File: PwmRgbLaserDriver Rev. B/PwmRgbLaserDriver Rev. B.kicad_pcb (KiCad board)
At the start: 2 copper layers, 63 x 42 mm, 55 parts, among them IC1 ADA4817-1ARDZ, IC2 ADA4817-1ARDZ, IC3 ADA4817-1ARDZ, J1 RED_IN, J2 15V, J3 RLO, J4 GREEN_IN, J5 GLO, J6 BLUE_IN, J7 BLO, Q1 Q_NPN_BCE, Q2 Q_NPN_BCE, Q3 Q_NPN_BCE, U1 TPS54331GDR

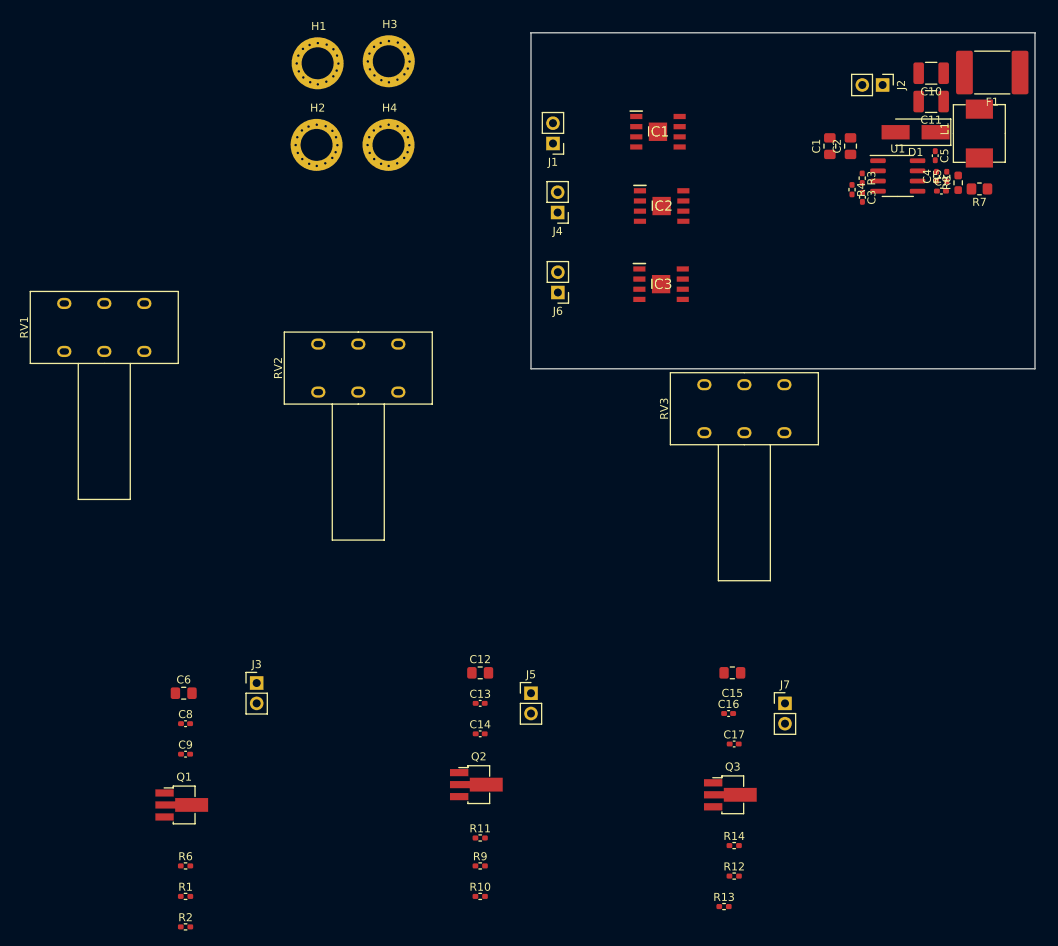
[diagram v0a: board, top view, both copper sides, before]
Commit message: Placement And Some Routhing
Placed all components and routed the important analog signal traces.
Power remains unfinished along with precise placement of the mounting holes.
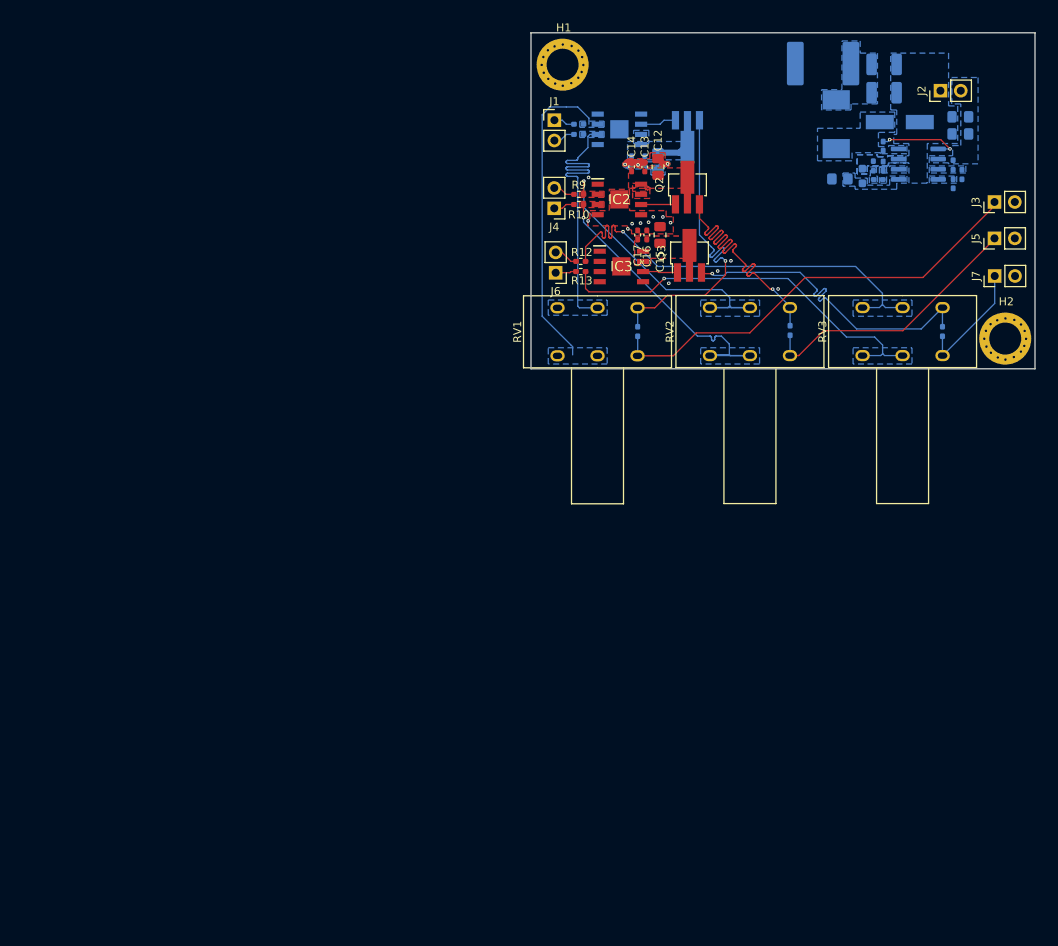
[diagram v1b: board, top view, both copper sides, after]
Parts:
- removed H3, H4: GND, SamacSys_Parts:4mm Mounting Hole
- C1, C10, C11, C2, C3, C4, C5, C6, C7, C8, C9, D1, F1, IC1, L1, Q1, R1, R11, R14, R2, R3, R4, R5, R6, R7, R8, U1: moved to B.Cu
- moved R2 111.7 mm to (213.0, 30.5)
- moved J3 110.1 mm to (264.9, 40.2), turned to 90 degrees
- moved R1 107.2 mm to (213.0, 31.8)
- moved Q1 104.7 mm to (226.6, 32.1), turned to 270 degrees
- moved C9 92.8 mm to (219.6, 35.1), turned to 270 degrees
- moved C8 90.8 mm to (221.2, 35.1), turned to 270 degrees
- moved H2 89.4 mm to (266.4, 52.2)
- moved C6 89.1 mm to (222.9, 35.1), turned to 270 degrees
- moved R6 87.5 mm to (220.3, 56.4), turned to 270 degrees
- moved R10 87.4 mm to (213.0, 40.5)
- moved R9 84.8 mm to (213.0, 39.2)
- moved R13 81.4 mm to (213.2, 48.9)
- moved J5 81.2 mm to (264.9, 44.7), turned to 90 degrees
- moved Q2 79.2 mm to (226.6, 38.4), turned to 90 degrees
- moved R12 79.2 mm to (213.2, 47.6)
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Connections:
- net Net-(J1-Pad1) renamed RIN
- net Net-(J4-Pad1) renamed GIN
- net Net-(J6-Pad1) renamed BIN
- IC1 pad 2: Net-(IC1-Pad2) -> ROA-IN
- IC1 pad 3: Net-(IC1-Pad3) -> ROA+IN
- IC2 pad 2: Net-(IC2-Pad2) -> GOA-IN
- IC2 pad 3: Net-(IC2-Pad3) -> GOA+IN
- IC3 pad 2: Net-(IC3-Pad2) -> BOA-IN
- IC3 pad 3: Net-(IC3-Pad3) -> BOA+IN
- IC3 pad 4: Net-(IC3-Pad4) -> GND
- IC3 pad 9: Net-(IC3-Pad4) -> GND
- J3 pad 1: Net-(J3-Pad1) -> RLO
- J5 pad 1: Net-(J5-Pad1) -> GLO
- J7 pad 1: Net-(J7-Pad1) -> BLO
- Q1 pad 3: Net-(Q1-Pad3) -> RQO
- Q2 pad 3: Net-(Q2-Pad3) -> GQO
- Q3 pad 3: Net-(Q3-Pad3) -> BQO
- R1 pad 2: Net-(IC1-Pad2) -> ROA-IN
- R10 pad 2: Net-(IC2-Pad3) -> GOA+IN
- R11 pad 1: Net-(Q2-Pad3) -> GQO
- R11 pad 2: Net-(J5-Pad1) -> GLO
- R12 pad 2: Net-(IC3-Pad2) -> BOA-IN
- R13 pad 2: Net-(IC3-Pad3) -> BOA+IN
- R14 pad 1: Net-(Q3-Pad3) -> BQO
- R14 pad 2: Net-(J7-Pad1) -> BLO
- R2 pad 2: Net-(IC1-Pad3) -> ROA+IN
- R6 pad 1: Net-(Q1-Pad3) -> RQO
- R6 pad 2: Net-(J3-Pad1) -> RLO
- R9 pad 2: Net-(IC2-Pad2) -> GOA-IN
- RV1 pad 1: Net-(IC1-Pad2) -> ROA+IN
- RV1 pad 2: Net-(IC1-Pad2) -> ROA+IN
- RV1 pad 3: Net-(Q1-Pad3) -> RLO
- RV1 pad 4: Net-(J3-Pad1) -> RQO
- RV1 pad 5: Net-(IC1-Pad3) -> ROA-IN
- RV1 pad 6: Net-(IC1-Pad3) -> ROA-IN
- RV2 pad 1: Net-(IC2-Pad2) -> GOA+IN
- RV2 pad 2: Net-(IC2-Pad2) -> GOA+IN
- RV2 pad 3: Net-(Q2-Pad3) -> GLO
- RV2 pad 4: Net-(J5-Pad1) -> GQO
- RV2 pad 5: Net-(IC2-Pad3) -> GOA-IN
- RV2 pad 6: Net-(IC2-Pad3) -> GOA-IN
- RV3 pad 1: Net-(IC3-Pad2) -> BOA+IN
- RV3 pad 2: Net-(IC3-Pad2) -> BOA+IN
- RV3 pad 3: Net-(Q3-Pad3) -> BLO
- RV3 pad 4: Net-(J7-Pad1) -> BQO
- RV3 pad 5: Net-(IC3-Pad3) -> BOA-IN
- RV3 pad 6: Net-(IC3-Pad3) -> BOA-IN
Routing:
- net RLO: track 0.00 -> 55.3 mm
- net BOA-IN: track 0.00 -> 55.1 mm, vias 0 -> 1
- net BOA+IN: track 0.00 -> 49.8 mm, vias 0 -> 1
- net BQO: track 0.00 -> 41.1 mm, vias 0 -> 1
- net RQO: track 0.00 -> 41.1 mm, vias 0 -> 1
- net GQO: track 0.00 -> 41.0 mm, vias 0 -> 1
- net ROA+IN: track 0.00 -> 39.2 mm
- net ROA-IN: track 0.00 -> 39.2 mm
- net GOA-IN: track 0.00 -> 39.1 mm, vias 0 -> 1
- net GOA+IN: track 0.00 -> 39.0 mm, vias 0 -> 1
- net GLO: track 0.00 -> 34.2 mm
- net GND: track 0.00 -> 15.2 mm, vias 0 -> 16
- net BLO: track 0.00 -> 15.1 mm
- net BOOT: track 0.00 -> 10.4 mm, vias 0 -> 2
- net +9V: track 0.00 -> 7.06 mm
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- added copper zone on B.Cu, net +15V
- added copper zone on B.Cu, net +9V
- added copper zone on F.Cu, net +9V
- added copper zone on B.Cu, net BOA+IN
- added copper zone on B.Cu, net BOA-IN
- added copper zone on B.Cu, net COMP
- added copper zone on B.Cu, net COMP_1
- added copper zone on B.Cu, net EN
- added copper zone on B.Cu, net GND
- added copper zone on F.Cu, net GND
- added copper zone on B.Cu, net GOA+IN
- added copper zone on F.Cu, net GOA+IN
- added copper zone on B.Cu, net GOA-IN
- added copper zone on F.Cu, net GOA-IN
- added copper zone on B.Cu, net PH
- added copper zone on B.Cu, net ROA+IN
- added copper zone on B.Cu, net ROA-IN
- added copper zone on B.Cu, net SS
- added copper zone on B.Cu, net VO
- added copper zone on B.Cu, net VSENSE
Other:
- copper layers 2 -> 4
- rule trace_min: 0.2 -> 0.127
- rule via_min_drill: 0.3 -> 0.2
- rule via_min_size: 0.4 -> 0.45

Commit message: Small Update
Nothing Much
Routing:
- net +9V: track 7.06 -> 13.7 mm
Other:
- outline, holes or cut-outs redrawn
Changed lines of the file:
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@@
   (general
     (thickness 0.8)
-    (drawings 4)
-    (tracks 735)
+    (drawings 6)
+    (tracks 738)
     (zones 0)
     (modules 53)
@@
   (page A4)
   (layers
-    (0 F.Cu signal)
+    (0 F.Cu signal hide)
     (1 In1.Cu power hide)
     (2 In2.Cu power hide)
-    (31 B.Cu signal)
+    (31 B.Cu signal hide)
     (32 B.Adhes user hide)
     (33 F.Adhes user hide)
     (34 B.Paste user hide)
     (35 F.Paste user hide)
-    (36 B.SilkS user)
-    (37 F.SilkS user)
-    (38 B.Mask user hide)
-    (39 F.Mask user hide)
+    (36 B.SilkS user hide)
+    (37 F.SilkS user hide)
+    (38 B.Mask user)
+    (39 F.Mask user)
     (40 Dwgs.User user hide)
     (41 Cmts.User user hide)
@@
     (tags "capacitor handsolder")
     (attr smd)
-    (fp_text reference C3 (at 0 1.16 270) (layer B.SilkS)
+    (fp_text reference C3 (at 1.8315 -0.058) (layer B.SilkS)
       (effects (font (size 1 1) (thickness 0.15)) (justify mirror))
     )
@@
     )
   )
-  (gr_line (start 207.01 19.05) (end 207.01 61.05) (layer Edge.Cuts) (width 0.05))
+  (gr_line (start 270.01 19.05) (end 207.645 19.05) (layer Edge.Cuts) (width 0.05))
+  (gr_line (start 207.01 19.685) (end 207.01 61.05) (layer Edge.Cuts) (width 0.05))
+  (gr_arc (start 207.645 19.685) (end 207.645 19.05) (angle -90) (layer Edge.Cuts) (width 0.05))
+  (gr_circle (center 269.367 60.452) (end 271.399 60.325) (layer Dwgs.User) (width 0.15))
   (gr_line (start 207.01 61.05) (end 270.01 61.05) (layer Edge.Cuts) (width 0.05))
   (gr_line (start 270.01 19.05) (end 270.01 61.05) (layer Edge.Cuts) (width 0.05))
-  (gr_line (start 207.01 19.05) (end 270.01 19.05) (layer Edge.Cuts) (width 0.05))
   (via (at 220.396 35.559) (size 0.45) (drill 0.2) (layers F.Cu B.Cu) (net 1))
   (via (at 218.769 35.504) (size 0.45) (drill 0.2) (layers F.Cu B.Cu) (net 1))
@@
   (segment (start 225.552 34.036) (end 222.885 34.036) (width 0.762) (layer B.Cu) (net 3))
   (segment (start 226.568 33.02) (end 225.552 34.036) (width 0.762) (layer B.Cu) (net 3))
+  (segment (start 226.822 48.9255) (end 226.822 46.355) (width 0.146812) (layer F.Cu) (net 3))
+  (segment (start 225.8275 45.3605) (end 223.139 45.3605) (width 0.146812) (layer F.Cu) (net 3))
+  (segment (start 226.822 46.355) (end 225.8275 45.3605) (width 0.146812) (layer F.Cu) (net 3))
   (segment (start 220.771 30.48) (end 223.139 30.48) (width 0.146812) (layer B.Cu) (net 4))
   (segment (start 223.638 29.981) (end 225.068 29.981) (width 0.146812) (layer B.Cu) (net 4))

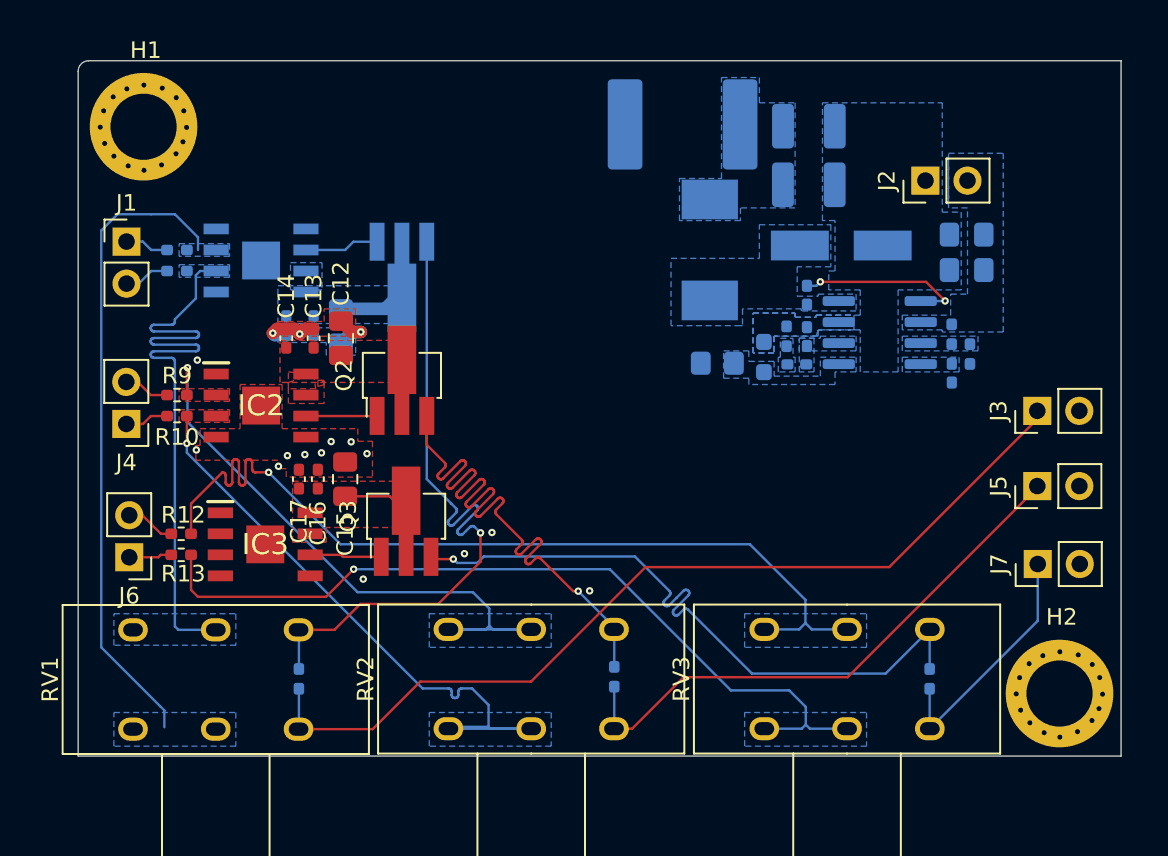
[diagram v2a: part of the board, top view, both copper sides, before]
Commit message: PDN Additions
All copper pours have been placed. Some PDN stitching vias have been placed.
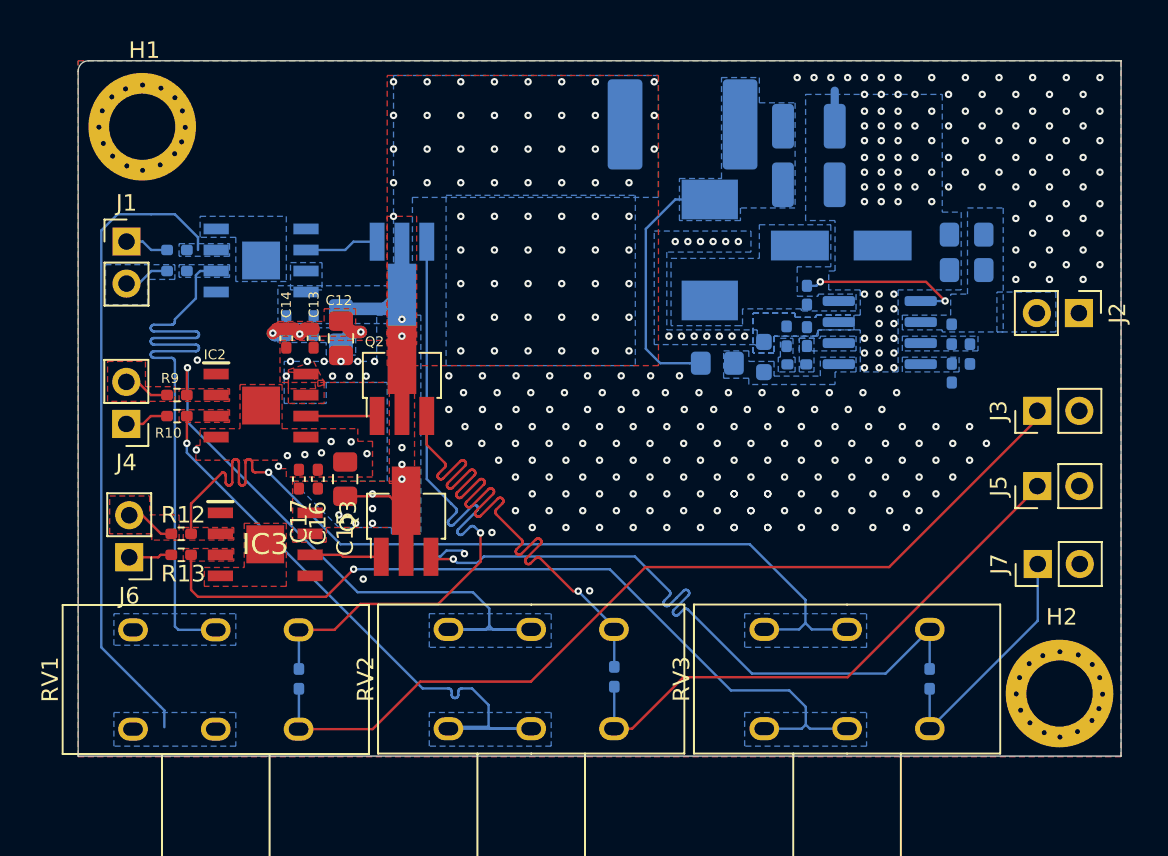
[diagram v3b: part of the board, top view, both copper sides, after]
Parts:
- moved J2 12.2 mm to (267.5, 34.3), turned to 270 degrees
- moved H1 0.08 mm to (211.0, 17.9)
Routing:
- net VO: track 0.00 -> 15.5 mm
- net GND: track 15.2 -> 19.3 mm, vias 16 -> 284
- net +9V: vias 0 -> 83
- added copper zone on F.Cu, net BOA+IN
- added copper zone on F.Cu, net BOA-IN
- added copper zone on In1.Cu, net GND
- added copper zone on In2.Cu, net GND

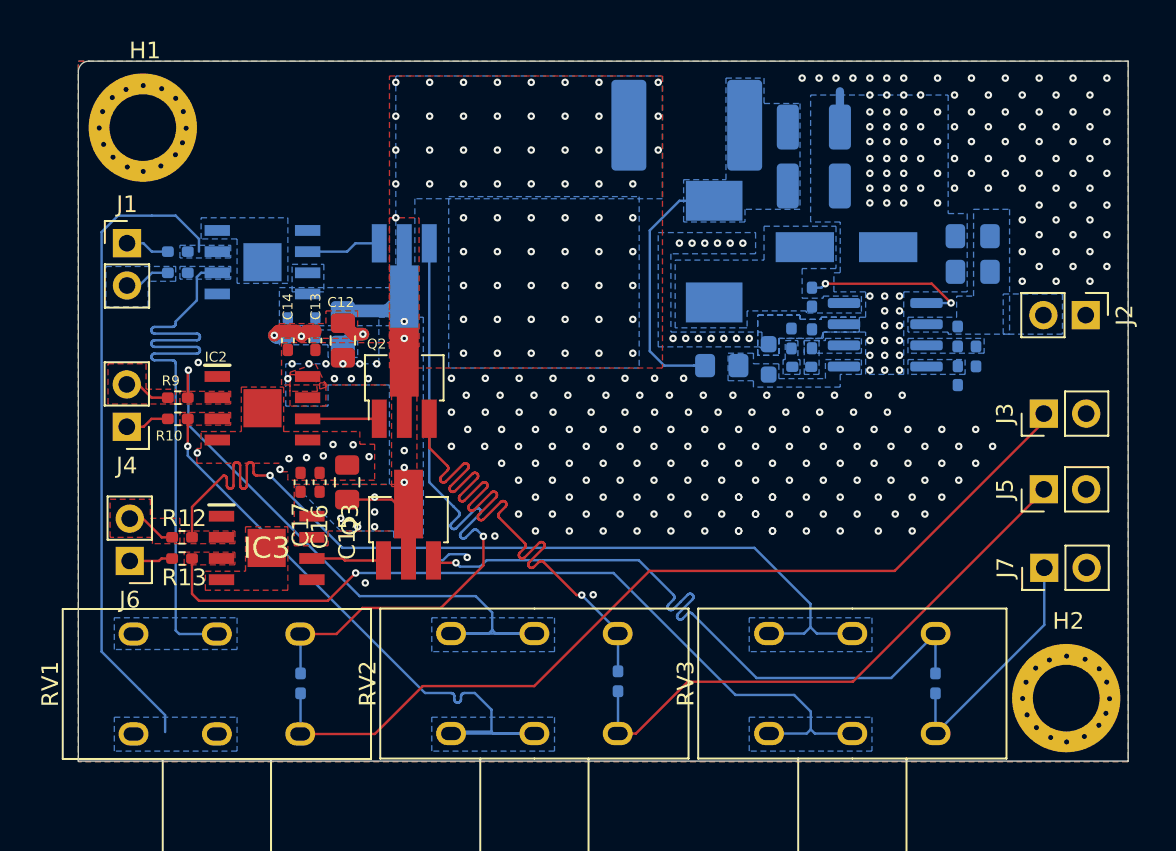
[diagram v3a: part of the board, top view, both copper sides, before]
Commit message: PDN & Silk Screen Improvements
Small additions
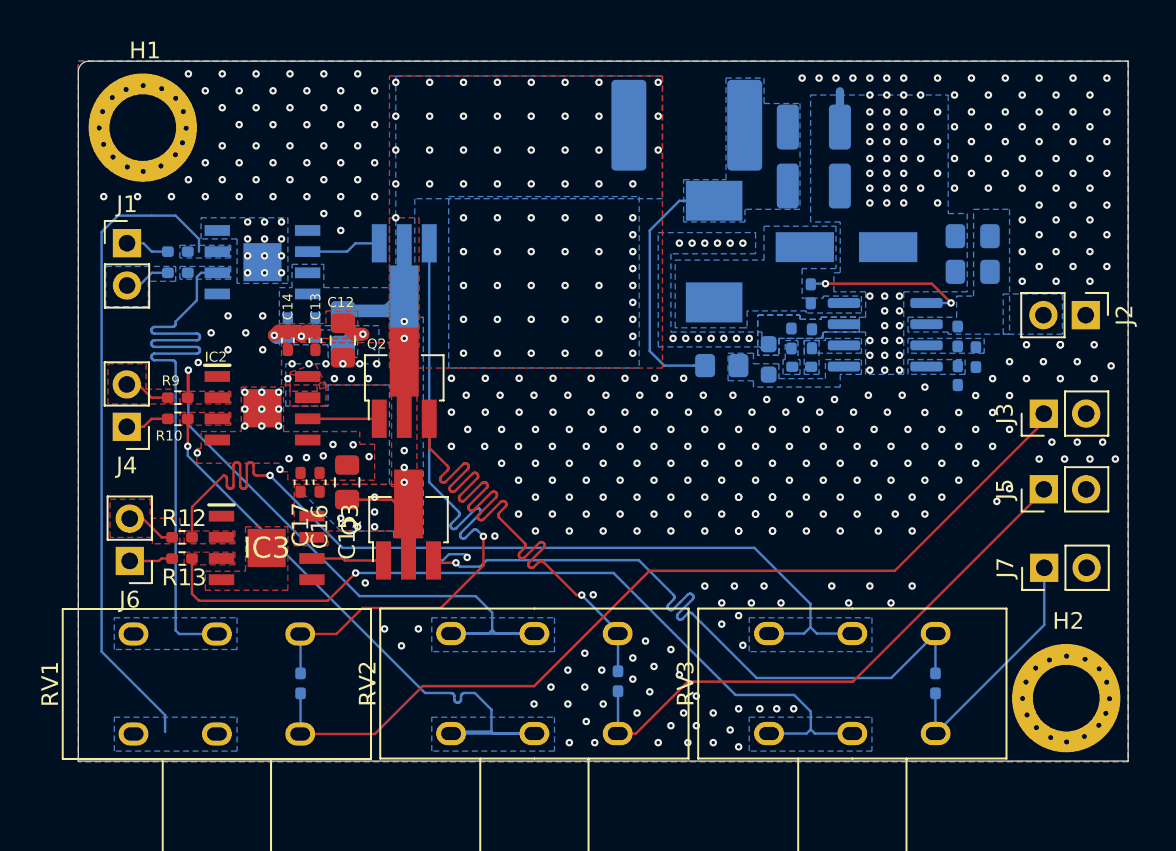
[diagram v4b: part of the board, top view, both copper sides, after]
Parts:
- added G***: LOGO, Custom Logos:OC_LOGO_5x5MM, B.Cu at (260.4, 49.0)
- moved C5 0.21 mm to (251.0, 33.0)
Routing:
- net GND: vias 284 -> 440
- net +9V: vias 83 -> 87
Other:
- board text added: "Blue"
- board text added: "Green"
- board text added: "JLCJLCJLCJLC"
- board text added: "Red"
- board text added: "Zach Walden 7/2021"
